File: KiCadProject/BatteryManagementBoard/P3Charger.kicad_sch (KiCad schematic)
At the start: 0 parts

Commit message: BQ25713 layout start
Signed-off-by: Eldalote.Electronics <Eldalote.Electronics@gmail.com>
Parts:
- added C? (x16): 10u, symbol Device:C
- added C? (x2): 47n, symbol Device:C
- added C? (x3): 1u, symbol Device:C
- added C? (x2): 33n, symbol Device:C
- added C?: 1n, symbol Device:C
- added C?: 100n, symbol Device:C
- added C?: 2u2, symbol Device:C
- added C?: 10n, symbol Device:C
- added L?: 2u2, symbol Device:L
- added Q? (x4): NFET_Gatenames, symbol Eldalote_symbols:NFET_Gatenames
- added Q?: PMOS_Gatenames, symbol Eldalote_symbols:PMOS_Gatenames
- added R? (x4): 10R, symbol Device:R
- added R? (x2): 10m, symbol Device:R
- added R? (x2): 4R99, symbol Device:R
- added U301: BQ25713, Package_DFN_QFN:Texas_S-PWQFN-N32_EP2.8x2.8mm, symbol Eldalote_symbols:BQ25713
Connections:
- new net: C?.1, R?.2, U301.7 (VDDA)
- new net: C?.2, C?.2, C?.2, C?.2, C?.2, C?.2, C?.2
- new net !BATDRV: Q?.G, U301.21 (!BATDRV)
- new net +BATT: C?.1, C?.2, R?.2, R?.2
- new net ACN: C?.1, R?.1, U301.2 (ACN)
- new net ACP: C?.1, R?.1, U301.3 (ACP)
- new net BTST1: C?.2, U301.30 (BTST1)
- new net BTST2: C?.2, U301.25 (BTST2)
- new net GND: C?.1, C?.1, C?.1, C?.1, C?.1, C?.1, C?.1, C?.1, C?.2, C?.2, C?.2, C?.2, C?.2, C?.2, C?.2, C?.2, C?.2, Q?.S, Q?.S, U301.27 (PGND), U301.33 (THERMALPAD)
- new net HIDRV1: Q?.G, U301.31 (HIDRV1)
- new net HIDRV2: Q?.G, U301.24 (HIDRV2)
- new net LODRV1: Q?.G, U301.29 (LODRV1)
- new net LODRV2: Q?.G, U301.26 (LODRV2)
- new net REGN: C?.1, R?.1, U301.28 (REGN)
- new net SRN: R?.1, U301.19 (SRN)
- new net SRP: R?.1, U301.20 (SRP)
- new net SW1: C?.1, L?.1, Q?.D, Q?.S, U301.32 (SW1)
- new net SW2: C?.1, L?.2, Q?.D, Q?.S, U301.23 (SW2)
- new net VBAT-ps: C?.1, C?.1, Q?.D, R?.1, R?.2
- new net VBUS: C?.1, C?.1, C?.1, C?.1, C?.1, C?.1, C?.1, R?.1, R?.1, R?.2
- new net VBUS-in: C?.1, R?.2, U301.1 (VBUS)
- new net VBUS-ps: C?.1, C?.1, Q?.D, R?.2, R?.2
- new net VSYS: C?.2, C?.2, C?.2, C?.2, C?.2, C?.2, C?.2, C?.2, Q?.D, Q?.S, U301.22 (VSYS)
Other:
- note added: "7x 10uF 25v"
- note added: "8x 10uF 25v"
- note added: "Buck-Boost Input Capacitors"
- note added: "Buck-Boost Output Capacitors"

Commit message: BQ25713 and LDO done? Stm32 next I think
Signed-off-by: Eldalote.Electronics <Eldalote.Electronics@gmail.com>
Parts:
- removed C?: 1u, symbol Device:C
- added C326: 1u, Capacitor_SMD:C_0603_1608Metric, symbol Device:C
- added C327: 33p, Capacitor_SMD:C_0402_1005Metric, symbol Device:C
- added C328: 1800p, Capacitor_SMD:C_0402_1005Metric, symbol Device:C
- added C329: 15p, Capacitor_SMD:C_0402_1005Metric, symbol Device:C
- added C330: 680p, Capacitor_SMD:C_0402_1005Metric, symbol Device:C
- added C332, C333: 100p, Capacitor_SMD:C_0402_1005Metric, symbol Device:C
- added R309, R312, R313: 100k, symbol Device:R
- added R310: 174k, symbol Device:R
- added R311: 300k, symbol Device:R
- added R314: 40K2, symbol Device:R
- added R315, R316, R317: 10k, symbol Device:R
- added R318: 137k, symbol Device:R
- C301, C302, C303, C304, C305, C306, C307, C314, C315, C317, C318, C319, C320, C321, C324: renamed from C?; footprint (none) -> Capacitor_SMD:C_0805_2012Metric
- C308, C309, C310, C311, C312, C313, C323: renamed from C?; footprint (none) -> Capacitor_SMD:C_0402_1005Metric
- C316, C322, C325, C331: renamed from C?; footprint (none) -> Capacitor_SMD:C_0603_1608Metric
- gave numbers to parts that had none: 14
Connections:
- net GND: now also U301.14 (CMPIN), C326.2, C327.2, C328.2, C329.2, C330.2, C332.2, C333.2, R311.1, R312.1, R313.1, R318.1
- net VDDA: now reaches R308.2, U301.7 (VDDA)
- net VDDA: now also C326.1, R309.2, R310.2
- net BQ_SDA: now reaches U301.12 (SDA)
- net BQ_SCL: now reaches U301.13 (SCL)
- net BQ_CMPOUT: now reaches U301.15 (CMPOUT)
- net BQ_CMPOUT: now also R317.1
- net COMP1: now reaches U301.16 (COMP1)
- net COMP1: now also C327.1, R314.2
- net COMP2: now reaches U301.17 (COMP2)
- net COMP2: now also C329.1, R315.2
- net CELL_BATPRESZ: now reaches U301.18 (CELL_BATPRESZ)
- net CELL_BATPRESZ: now also R309.1, R311.2
- net BQ_CHRG_OK: now reaches U301.4 (CHRG_OK)
- net BQ_CHRG_OK: now also R316.1
- net BQ_EN_OTG: now reaches U301.5 (OTG/VAP)
- net BQ_EN_OTG: now also R313.2
- net at U301.6 (ILIM_HIZ): now also R310.1, R312.2
- net BQ_IADPT: now reaches U301.8 (IADPT)
- net BQ_IADPT: now also C332.1, R318.2
- net BQ_IBAT: now reaches U301.9 (IBAT)
- net BQ_IBAT: now also C333.1
- net VSYS renamed VOUT
- new net +3.3V: R316.2, R317.2
- new net COMP1RC: C328.1, R314.1
- new net COMP2RC: C330.1, R315.1
- no-connect marks 0 -> 2
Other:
- note added: "BQ25713 Battery Charger"
- note added: "Battery and power adaptor current output Clamped at 3.3V 137k corresponds with 2.2uH inductor"
- note added: "For 3A USB in current limit ILIM_HIZ should be at 2.2V (VIlim) VIlim = 1v + (40 * Ilim * RAC) RAC = 10mOhm, Ilim = 3A VIlim = 1v + (40 * 3 * 0.01) = 2.2V VDDA is regulated to 6V Divider with closest normal values: 174k over 100k (2.19V)"
- note added: "For a 4S Battery CELL_BATPRESZ should be at roughly 75% of VDDA"
- note added: "INTER SHEET CONNECTIVITY"
- note added: "Place compensation network close to sense resistor per datasheet"
- note added: "Place further at least 2x 22uF elec caps at load for Vsys (present at LED driver board, connectors and regulator)"
- note added: "To LED driver connector (Page 2) and 3v3 regulator (Page 6)"
- note added: "To STM32 (Page 4)"
- note added: "VDDA decouple"
- moved on the sheet: C325, C331, R307, R308, U301A

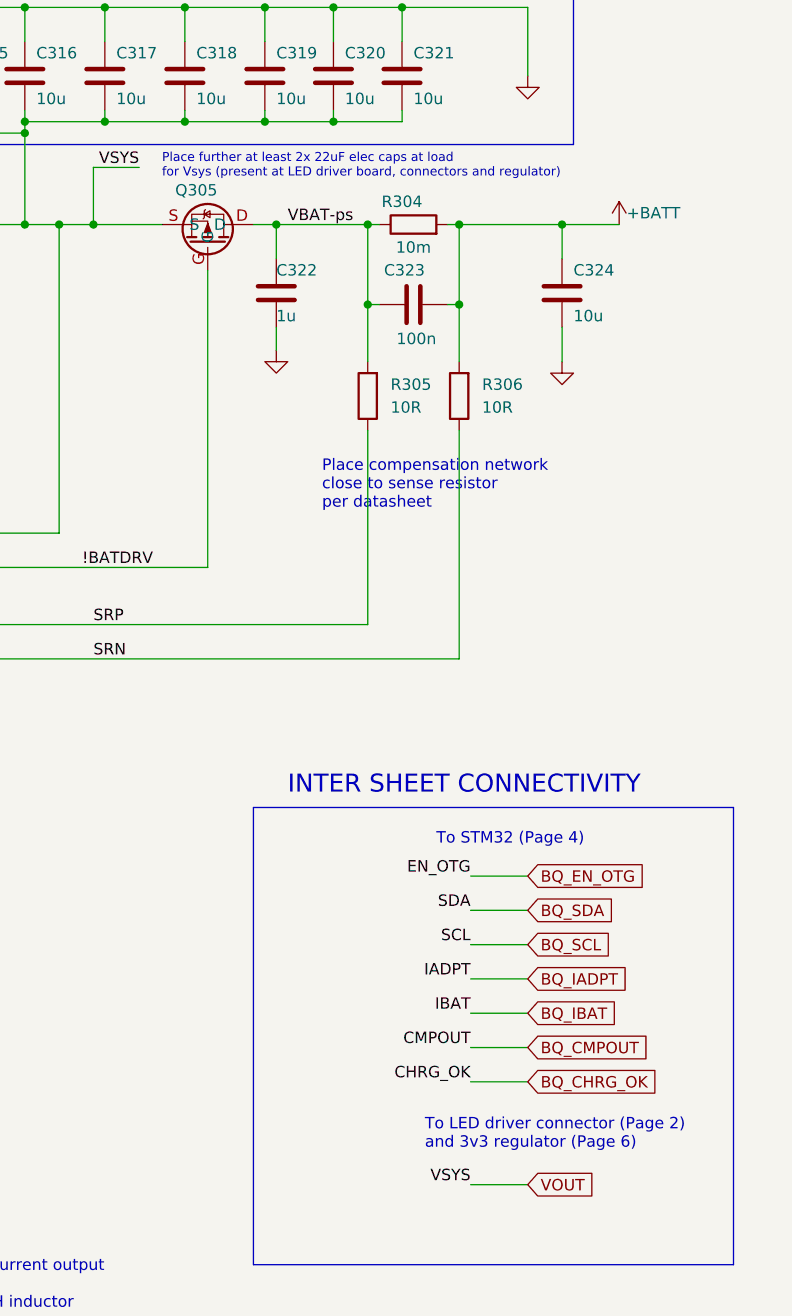
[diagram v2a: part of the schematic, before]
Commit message: Change to design: No more STM32, just use resistors for USB-C PD, en move the battery cell measuring and leveling to the other board.
Signed-off-by: Eldalote.Electronics <Eldalote.Electronics@gmail.com>
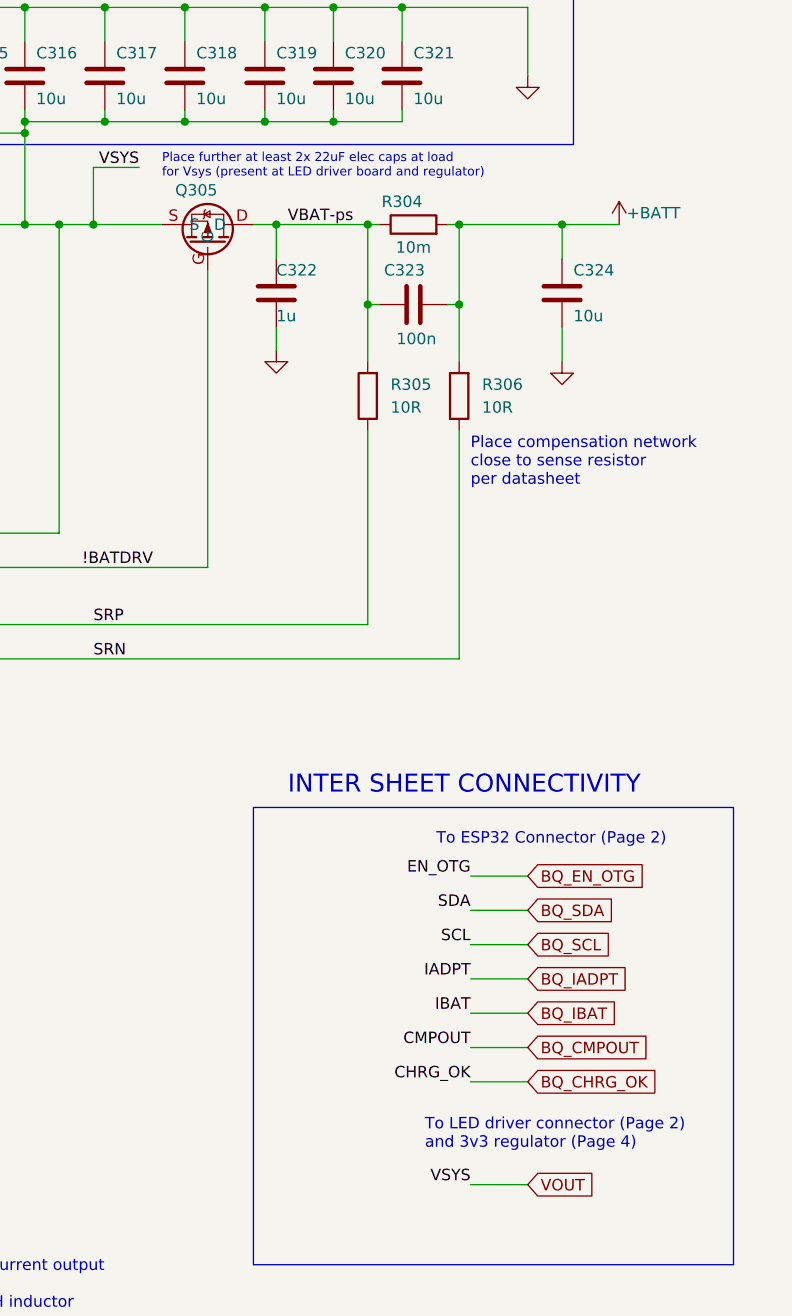
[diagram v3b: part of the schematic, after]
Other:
- note added: "Place further at least 2x 22uF elec caps at load for Vsys (present at LED driver board and regulator)"
- note added: "To ESP32 Connector (Page 2)"
- note added: "To LED driver connector (Page 2) and 3v3 regulator (Page 4)"
- note removed: "Place further at least 2x 22uF elec caps at load for Vsys (present at LED driver board, connectors and regulator)"
- note removed: "To LED driver connector (Page 2) and 3v3 regulator (Page 6)"
- note removed: "To STM32 (Page 4)"
- company: (none) -> Eldalote Electronics
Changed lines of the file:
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@@
 (kicad_sch (version 20211123) (generator eeschema)
   (paper "A4")
+  (title_block
+    (rev "0.1")
+    (company "Eldalote Electronics")
+  )
   (junction (at 45.72 60.96) (diameter 0) (color 0 0 0 0)
   )
@@
     (stroke (width 0) (type default) (color 0 0 0 0))
   )
-  (text "To LED driver connector (Page 2)\nand 3v3 regulator (Page 6)\n"
+  (text "To LED driver connector (Page 2)\nand 3v3 regulator (Page 4)\n"
     (at 245.11 146.05 0)
     (effects (font (size 1.27 1.27)) (justify left bottom))
@@
     (effects (font (size 1.27 1.27)) (justify left bottom))
   )
-  (text "Place further at least 2x 22uF elec caps at load\nfor Vsys (present at LED driver board, connectors and regulator)"
+  (text "Place further at least 2x 22uF elec caps at load\nfor Vsys (present at LED driver board and regulator)"
     (at 215.9 38.1 0)
     (effects (font (size 1 1)) (justify left bottom))
@@
     (effects (font (size 1.27 1.27)) (justify left bottom))
   )
-  (text "To STM32 (Page 4)\n\n" (at 246.38 114.3 0)
+  (text "To ESP32 Connector (Page 2)\n\n" (at 246.38 114.3 0)
     (effects (font (size 1.27 1.27)) (justify left bottom))
   )
   (text "Place compensation network\nclose to sense resistor\nper datasheet\n"
-    (at 233.68 74.93 0)
+    (at 250.19 72.39 0)
     (effects (font (size 1.27 1.27)) (justify left bottom))
   )

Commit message: jan 4
Signed-off-by: Eldalote.Electronics <Eldalote.Electronics@gmail.com>
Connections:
- net GND: now also C301.2, C302.2, C303.2, C304.2, C305.2, C306.2, C307.2
- net BQ_SCL renamed SCL
- net BQ_SDA renamed SDA
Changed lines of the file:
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@@
     )
   )
-  (global_label "BQ_SCL" (shape input) (at 256.54 123.19 0) (fields_autoplaced)
+  (global_label "SCL" (shape input) (at 256.54 123.19 0) (fields_autoplaced)
     (effects (font (size 1.27 1.27)) (justify left))
-    (property "Intersheet References" "${INTERSHEET_REFS}" (id 0) (at 266.0288 123.1106 0)
+    (property "Intersheet References" "${INTERSHEET_REFS}" (id 0) (at 262.4607 123.1106 0)
       (effects (font (size 1.27 1.27)) (justify left) hide)
     )
@@
     )
   )
-  (global_label "BQ_SDA" (shape input) (at 256.54 119.38 0) (fields_autoplaced)
+  (global_label "SDA" (shape input) (at 256.54 119.38 0) (fields_autoplaced)
     (effects (font (size 1.27 1.27)) (justify left))
-    (property "Intersheet References" "${INTERSHEET_REFS}" (id 0) (at 266.0893 119.3006 0)
+    (property "Intersheet References" "${INTERSHEET_REFS}" (id 0) (at 262.5212 119.3006 0)
       (effects (font (size 1.27 1.27)) (justify left) hide)
     )
@@
     (pin "2")
   )
-  (symbol (lib_id "power:GND") (at 50.8 62.23 0) (unit 1)
+  (symbol (lib_id "power:GND") (at 45.72 62.23 0) (unit 1)
     (in_bom yes) (on_board yes) (fields_autoplaced)
-    (property "Reference" "#PWR0303" (id 0) (at 50.8 68.58 0)
+    (property "Reference" "#PWR0303" (id 0) (at 45.72 68.58 0)
       (effects (font (size 1.27 1.27)) hide)
     )
-    (property "Value" "GND" (id 1) (at 50.8 67.31 0)
+    (property "Value" "GND" (id 1) (at 45.72 67.31 0)
       (effects (font (size 1.27 1.27)) hide)
     )
-    (property "Footprint" "" (id 2) (at 50.8 62.23 0)
+    (property "Footprint" "" (id 2) (at 45.72 62.23 0)
       (effects (font (size 1.27 1.27)) hide)
     )
-    (property "Datasheet" "" (id 3) (at 50.8 62.23 0)
+    (property "Datasheet" "" (id 3) (at 45.72 62.23 0)
       (effects (font (size 1.27 1.27)) hide)
     )
